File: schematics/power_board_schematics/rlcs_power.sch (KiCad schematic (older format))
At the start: 40 parts, among them J1 SD_Card, J2 Battery Conn, J3 CONN_01X02, J4 CONN_01X02, J5 CONN_01X02, J6 CONN_01X02, Q4 Q_NPN_BEC, Q5 Q_NPN_BEC, T1 12 to 3v3, T2 12 to 5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

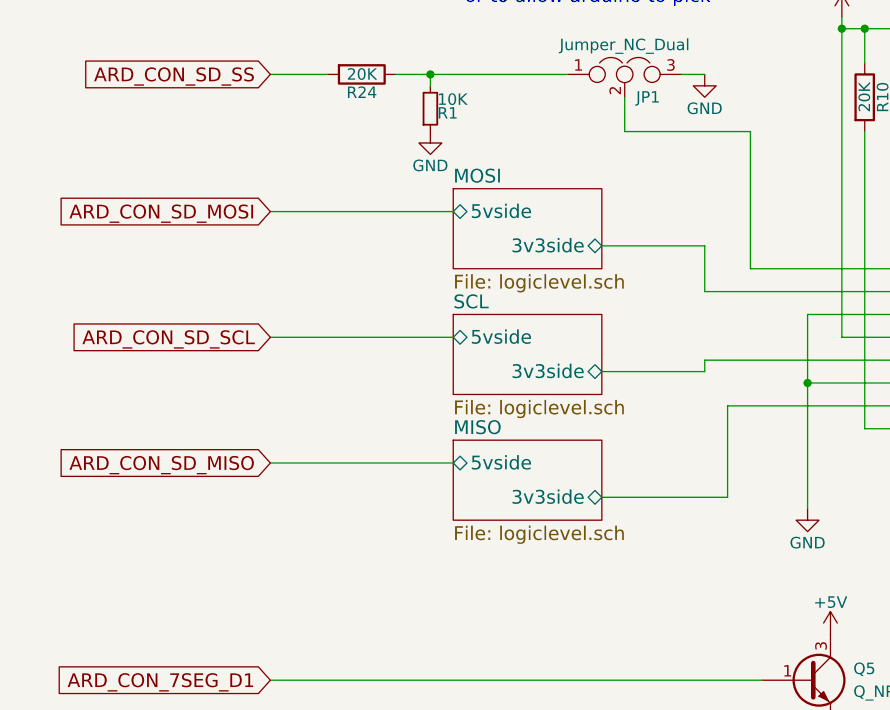
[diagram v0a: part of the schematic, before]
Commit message: Replace bidirectional shifter for SD card
Now MOSI and SCL run through voltage dividers, and MISO is just a wire.
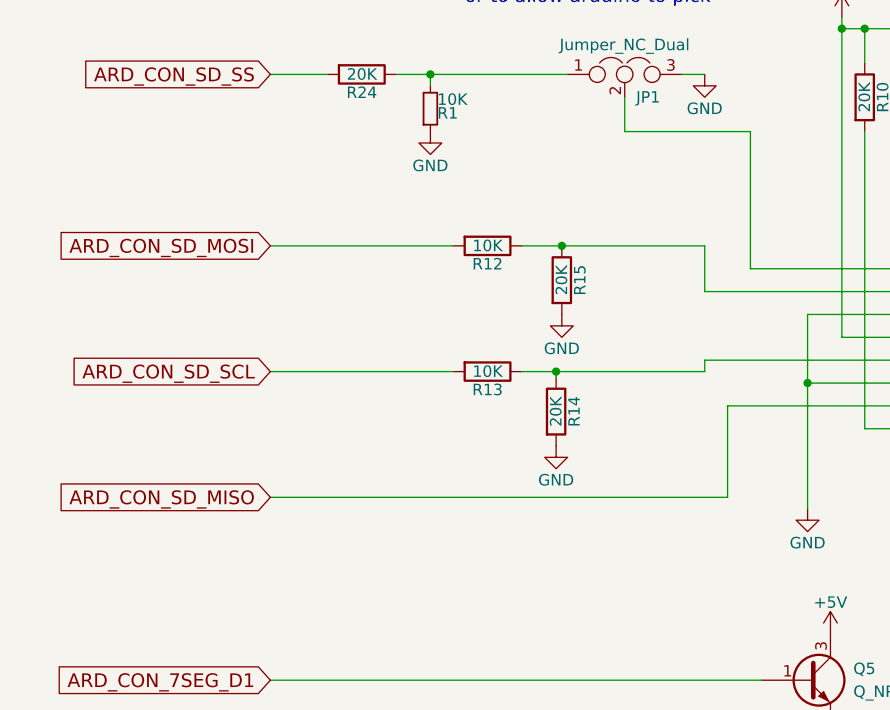
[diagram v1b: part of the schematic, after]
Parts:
- added R12, R13: 10K, Resistors_SMD:R_0805_HandSoldering, symbol R
- added R14, R15: 20K, Resistors_SMD:R_0805_HandSoldering, symbol R
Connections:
- net MISO/3v3side is gone; now on net ARD_CON_SD_MISO: J1.7 (DAT0)
- net ARD_CON_SD_MOSI: now also R12.2
- net ARD_CON_SD_SCL: now also R13.2
- net GND: now also R14.2, R15.2
- net MOSI/3v3side: no longer names the net of J1.2 (CMD)
- net MOSI/3v3side: now also R12.1, R15.1
- net SCL/3v3side: no longer names the net of J1.5 (CLK)
- net SCL/3v3side: now also R13.1, R14.1
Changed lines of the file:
@@
 $Descr A4 11693 8268
 encoding utf-8
-Sheet 1 5
+Sheet 1 2
 Title "RLCS power board"
 Date "2017-09-24"
@@
 	1    0    0    -1
 $EndComp
-$Sheet
-S 2750 1750 650  350
-U 59B5D8D3
-F0 "MOSI" 60
-F1 "logiclevel.sch" 60
-F2 "3v3side" B R 3400 2000 60
-F3 "5vside" B L 2750 1850 60
-$EndSheet
-$Sheet
-S 2750 2300 650  350
-U 59B5E10D
-F0 "SCL" 60
-F1 "logiclevel.sch" 60
-F2 "3v3side" B R 3400 2550 60
-F3 "5vside" B L 2750 2400 60
-$EndSheet
-$Sheet
-S 2750 2850 650  350
-U 59B5E16A
-F0 "MISO" 60
-F1 "logiclevel.sch" 60
-F2 "3v3side" B R 3400 3100 60
-F3 "5vside" B L 2750 2950 60
-$EndSheet
 $Comp
 L GND #PWR010
@@
 Text GLabel 1950 1250 0    60   Input ~ 0
 ARD_CON_SD_SS
-Text GLabel 1950 1850 0    60   Input ~ 0
+Text GLabel 1950 2000 0    60   Input ~ 0
 ARD_CON_SD_MOSI
-Text GLabel 1950 2400 0    60   Input ~ 0
+Text GLabel 1950 2550 0    60   Input ~ 0
 ARD_CON_SD_SCL
-Text GLabel 1950 2950 0    60   Input ~ 0
+Text GLabel 1950 3100 0    60   Input ~ 0
 ARD_CON_SD_MISO
 Text GLabel 1950 3900 0    60   Input ~ 0
@@
 	3850 2000 3850 2200
 Wire Wire Line
-	3850 2000 3400 2000
+	3050 2000 3850 2000
 Wire Wire Line
 	4300 2300 4850 2300
@@
 	3850 2200 4850 2200
 Wire Wire Line
-	3400 2550 3850 2550
+	3050 2550 3850 2550
 Wire Wire Line
 	3850 2550 3850 2500
@@
 	3950 2700 4850 2700
 Wire Wire Line
-	3950 2700 3950 3100
-Wire Wire Line
-	3950 3100 3400 3100
+	3950 3100 3950 2700
+Wire Wire Line
+	1950 3100 3950 3100
 Wire Wire Line
 	4450 1000 4450 2400
@@
 	3500 1500 3500 1350
 Wire Wire Line
-	1950 1850 2750 1850
-Wire Wire Line
-	1950 2400 2750 2400
-Wire Wire Line
-	1950 2950 2750 2950
+	1950 2000 2750 2000
+Wire Wire Line
+	1950 2550 2750 2550
 Wire Wire Line
 	2000 4900 3350 4900
@@
 $EndComp
 Connection ~ 9575 3450
+$Comp
+L R R15
+U 1 1 5A5952A0
+P 3225 2150
+F 0 "R15" V 3305 2150 50  0000 C CNN
+F 1 "20K" V 3225 2150 50  0000 C CNN
+F 2 "Resistors_SMD:R_0805_HandSoldering" V 3155 2150 50  0001 C CNN
+F 3 "" H 3225 2150 50  0001 C CNN
+	1    3225 2150
+	1    0    0    -1
+$EndComp
+$Comp
+L R R14
+U 1 1 5A595360
+P 3200 2725
+F 0 "R14" V 3280 2725 50  0000 C CNN
+F 1 "20K" V 3200 2725 50  0000 C CNN
+F 2 "Resistors_SMD:R_0805_HandSoldering" V 3130 2725 50  0001 C CNN
+F 3 "" H 3200 2725 50  0001 C CNN
+	1    3200 2725
+	1    0    0    -1
+$EndComp
+$Comp
+L GND #PWR027
+U 1 1 5A595401
+P 3200 2875
+F 0 "#PWR027" H 3200 2625 50  0001 C CNN
+F 1 "GND" H 3200 2725 50  0000 C CNN
+F 2 "" H 3200 2875 50  0001 C CNN
+F 3 "" H 3200 2875 50  0001 C CNN
+	1    3200 2875
+	1    0    0    -1
+$EndComp
+$Comp
+L GND #PWR028
+U 1 1 5A59548A
+P 3225 2300
+F 0 "#PWR028" H 3225 2050 50  0001 C CNN
+F 1 "GND" H 3225 2150 50  0000 C CNN
+F 2 "" H 3225 2300 50  0001 C CNN
+F 3 "" H 3225 2300 50  0001 C CNN
+	1    3225 2300
+	1    0    0    -1
+$EndComp
+Wire Wire Line
+	3200 2550 3200 2575
+$Comp
+L R R12
+U 1 1 5A596C23
+P 2900 2000
+F 0 "R12" V 2980 2000 50  0000 C CNN
+F 1 "10K" V 2900 2000 50  0000 C CNN
+F 2 "Resistors_SMD:R_0805_HandSoldering" V 2830 2000 50  0001 C CNN
+F 3 "" H 2900 2000 50  0001 C CNN
+	1    2900 2000
+	0    1    1    0
+$EndComp
+$Comp
+L R R13
+U 1 1 5A596E89
+P 2900 2550
+F 0 "R13" V 2980 2550 50  0000 C CNN
+F 1 "10K" V 2900 2550 50  0000 C CNN
+F 2 "Resistors_SMD:R_0805_HandSoldering" V 2830 2550 50  0001 C CNN
+F 3 "" H 2900 2550 50  0001 C CNN
+	1    2900 2550
+	0    1    1    0
+$EndComp
+Connection ~ 3225 2000
+Connection ~ 3200 2550
 $EndSCHEMATC

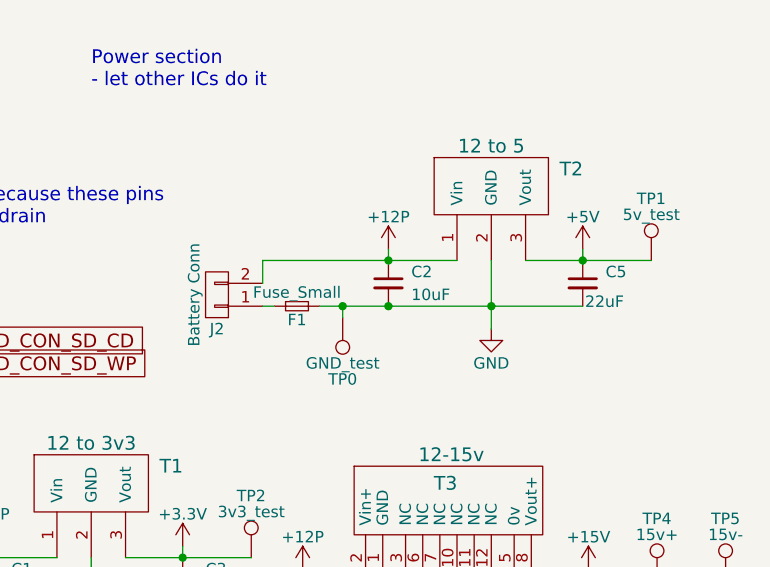
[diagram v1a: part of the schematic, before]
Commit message: Change fusing from bottom side to top side
Correct that error. Also add flyback diode to relay board
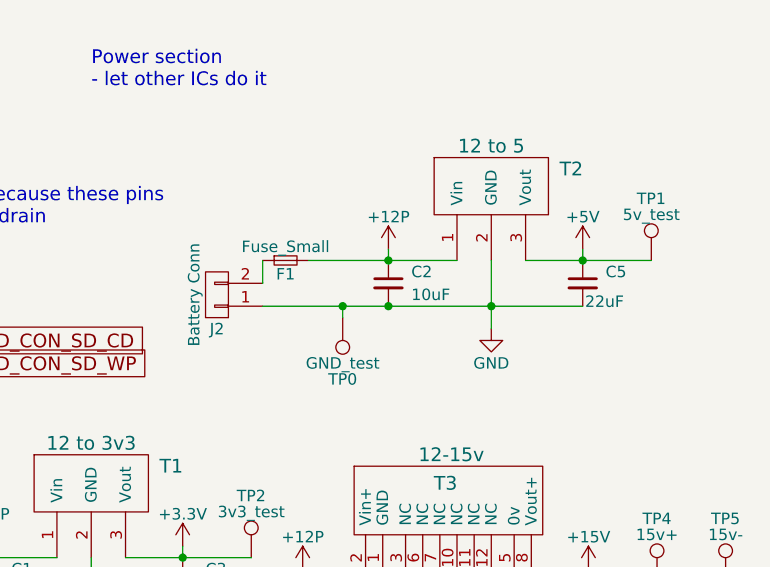
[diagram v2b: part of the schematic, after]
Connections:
- net +12P: now also F1.2; no longer J2.2 (P2)
- net GND: now also J2.1 (P1); no longer F1.2
- net at F1.1: now also J2.2 (P2); no longer J2.1 (P1)
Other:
- moved on the sheet: F1
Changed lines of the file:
@@
 L Fuse_Small F1
 U 1 1 59B5BFB2
-P 9200 2050
-F 0 "F1" H 9200 1990 50  0000 C CNN
-F 1 "Fuse_Small" H 9200 2110 50  0000 C CNN
-F 2 "Fuse_Holders_and_Fuses:Fuseholder5x20_horiz_open_inline_Type-I" H 9200 2050 50  0001 C CNN
-F 3 "" H 9200 2050 50  0001 C CNN
-	1    9200 2050
+P 9150 1850
+F 0 "F1" H 9150 1790 50  0000 C CNN
+F 1 "Fuse_Small" H 9150 1910 50  0000 C CNN
+F 2 "Fuse_Holders_and_Fuses:Fuseholder5x20_horiz_open_inline_Type-I" H 9150 1850 50  0001 C CNN
+F 3 "" H 9150 1850 50  0001 C CNN
+	1    9150 1850
 	1    0    0    -1
 $EndComp
@@
 Connection ~ 10050 2050
 Wire Wire Line
-	9050 1850 9900 1850
-Wire Wire Line
 	9050 1850 9050 1950
 Wire Wire Line
@@
 Connection ~ 2650 1250
 Wire Wire Line
-	9050 2050 9100 2050
-Wire Wire Line
-	9300 2050 10450 2050
+	9050 2050 10450 2050
 Wire Wire Line
 	9225 3250 9500 3250
@@
 Connection ~ 3225 2000
 Connection ~ 3200 2550
+Wire Wire Line
+	9250 1850 9900 1850
 $EndSCHEMATC
